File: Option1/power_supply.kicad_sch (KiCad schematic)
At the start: 26 parts, among them U201 uA7812, U202 K7805-500R2_C909663, U203 SY8089AAAC

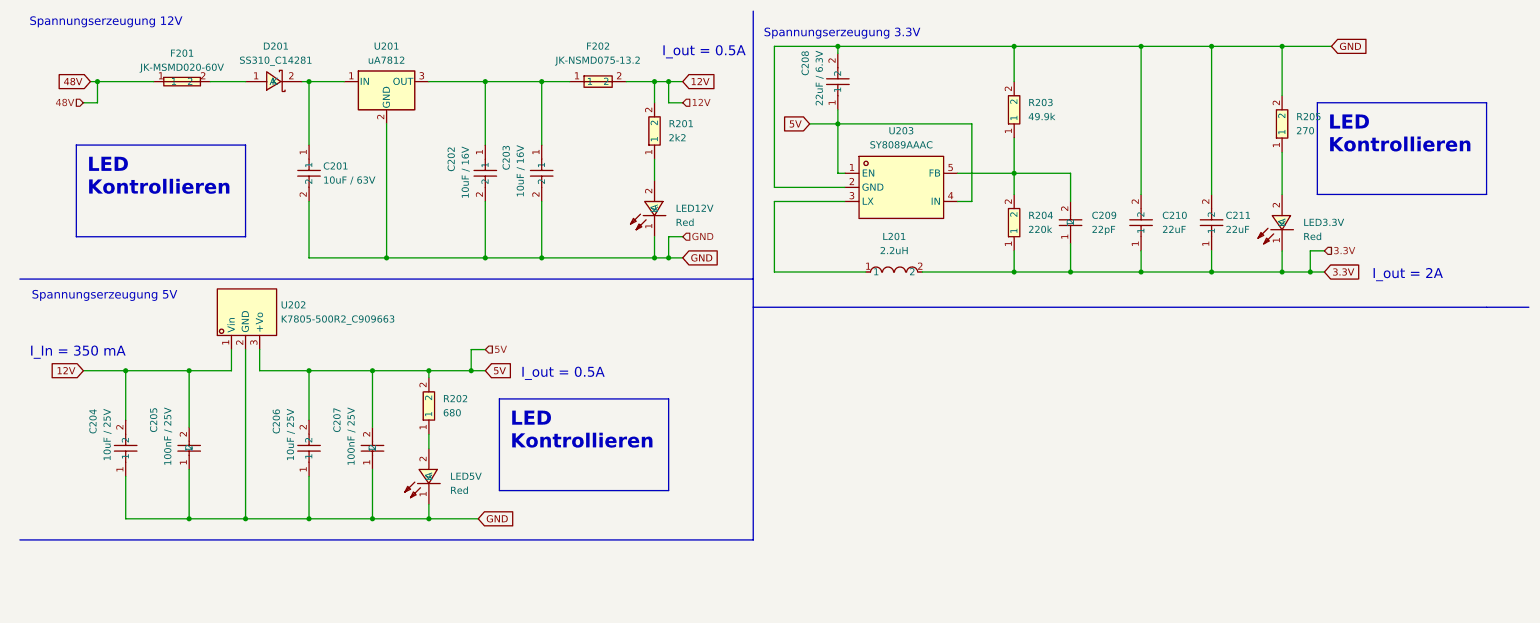
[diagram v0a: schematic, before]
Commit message: SPI Flash hinzugefügt, IN/Outputs vereinheitlicht, USB Flash Möglichkeit hinzugefügt, Display fehtl noch
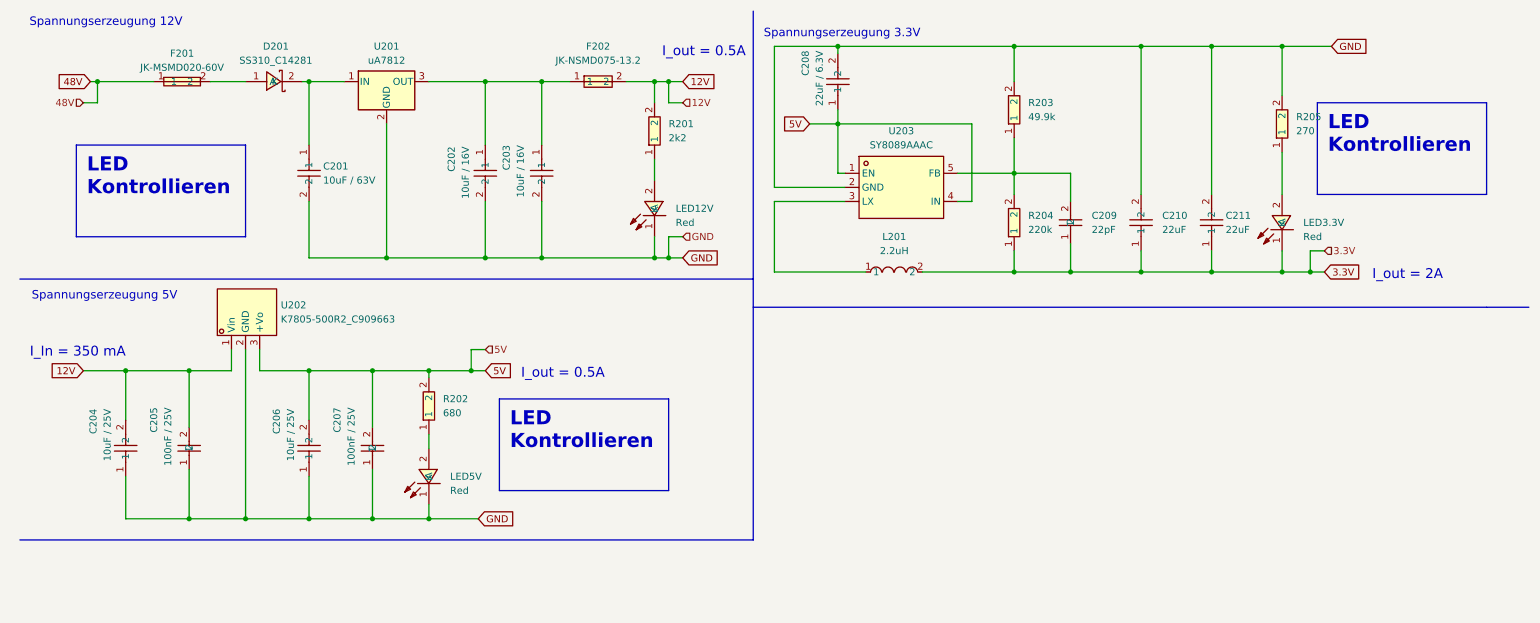
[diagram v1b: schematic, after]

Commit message: Erste issues eingearbeitet
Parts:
- removed LED12V, LED3.3V, LED5V: Red, easyeda2kicad:LED0603-RD, symbol easyeda2kicad:KT-0603R
- removed R201: 2k2, easyeda2kicad:R0603, symbol easyeda2kicad:0603WAF2201T5E
- removed R202: 680, easyeda2kicad:R0603, symbol easyeda2kicad:0603WAF6800T5E
- removed R205: 270, easyeda2kicad:R0603, symbol easyeda2kicad:0603WAF2700T5E
- removed U201: uA7812, symbol Regulator_Linear:uA7812
- added LED12V, LED3V3, LED5V: XL-1608SYGC-06, easyeda2kicad:LED0603-RD_GREEN, symbol EasyEda2KiCad:XL-1608SYGC-06
- added R201: 1.8kΩ, easyeda2kicad:R0603, symbol EasyEda2KiCad:0603WAF1801T5E
- added R202: 560Ω, easyeda2kicad:R0603, symbol EasyEda2KiCad:0603WAF5600T5E
- added R205: 220Ω, easyeda2kicad:R0603, symbol EasyEda2KiCad:0603WAJ0221T5E
- added U201: U7812-500, easyeda2kicad:PWRM-TH_3P-L11.6-W9.0-P2.54, symbol EasyEda2KiCad:U7812-500
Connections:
- net 12V: now also R201.2
- net 3.3V: now also LED3V3.1 (K)
- net 5V: now also R202.2
- net GND: now also LED12V.1 (K), LED5V.1 (K), R205.2, U201.2 (GND)
- net 12V_OUT: now reaches C202.1, C203.1, F202.1
- net 12V_OUT: now also U201.3 (Vout)
- net 48V_FUSED: now reaches C201.1, D201.2 (K)
- net 48V_FUSED: now also U201.1 (Vin)
- new net: LED3V3.2 (A), R205.1
- new net: LED5V.2 (A), R202.1
- new net: LED12V.2 (A), R201.1
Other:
- note added: "5mA - Green"
- moved on the sheet: D201

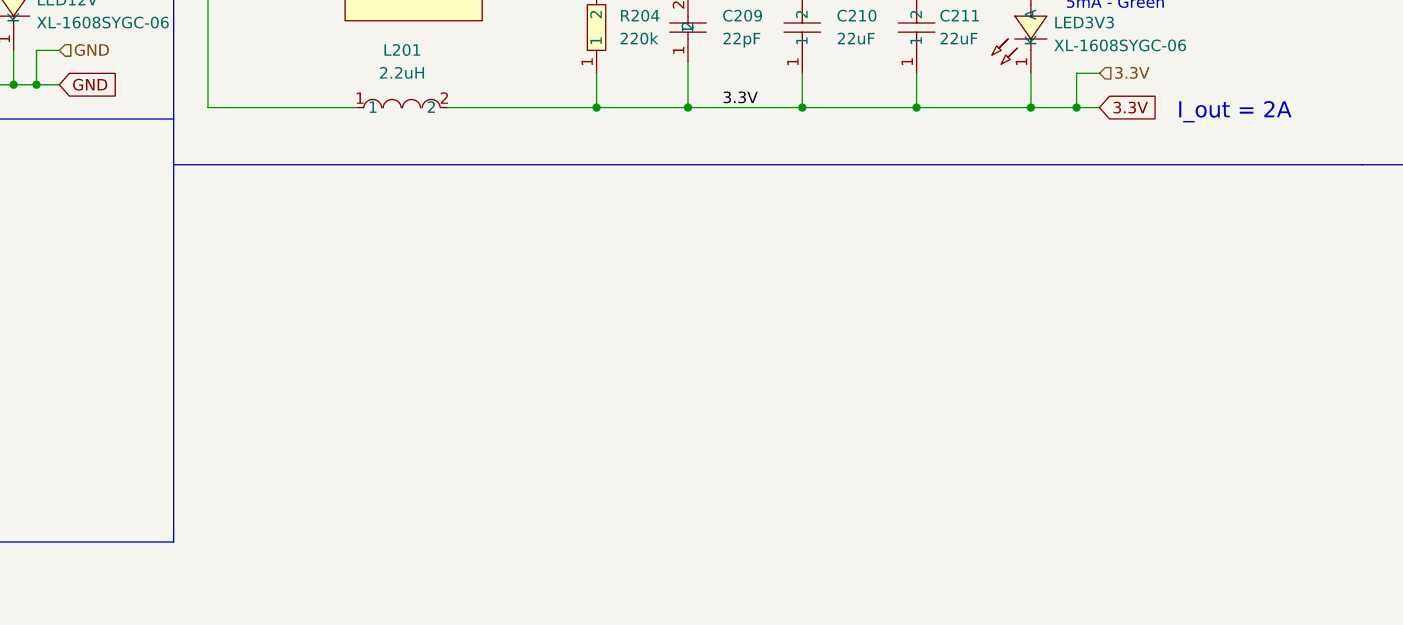
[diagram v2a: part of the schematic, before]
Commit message: Zweite 3V3 Spannungsversorgung für Display hinzugefügt
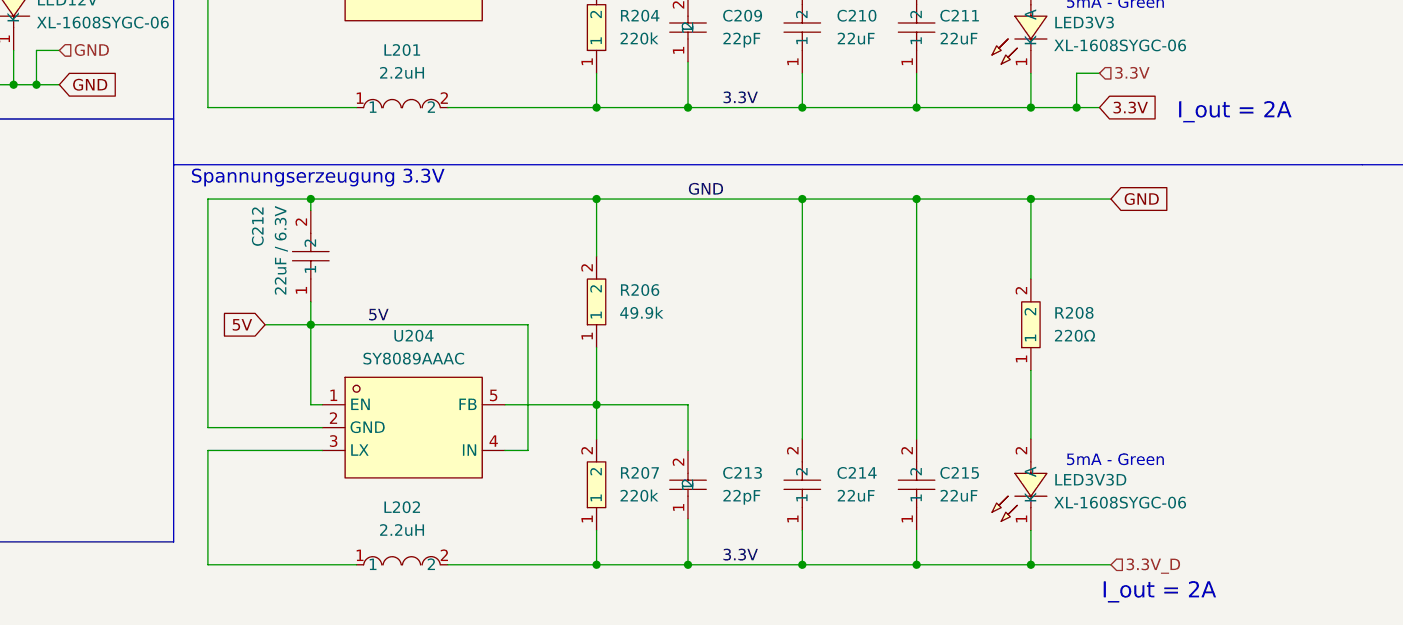
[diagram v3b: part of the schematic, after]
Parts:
- added C212: 22uF / 6.3V, easyeda2kicad:C0603, symbol easyeda2kicad:CL10A226MQ8NRNC
- added C213: 22pF, easyeda2kicad:C0805, symbol easyeda2kicad:CL21C220JBANNNC
- added C214, C215: 22uF, easyeda2kicad:C0805, symbol easyeda2kicad:CL21A226MAQNNNE
- added L202: 2.2uH, easyeda2kicad:IND-SMD_L3.0-W3.0_NR3010, symbol easyeda2kicad:NR3015T2R2M
- added LED3V3D: XL-1608SYGC-06, easyeda2kicad:LED0603-RD_GREEN, symbol EasyEda2KiCad:XL-1608SYGC-06
- added R206: 49.9k, easyeda2kicad:R0603, symbol easyeda2kicad:0603WAF4992T5E
- added R207: 220k, easyeda2kicad:R0603, symbol easyeda2kicad:0603WAF2203T5E
- added R208: 220Ω, easyeda2kicad:R0603, symbol EasyEda2KiCad:0603WAJ0221T5E
- added U204: SY8089AAAC, easyeda2kicad:SOT-23-5_L3.0-W1.7-P0.95-LS2.8-BR, symbol easyeda2kicad:SY8089AAAC
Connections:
- net 3.3V: now also C213.1, C214.1, C215.1, L202.2, LED3V3D.1 (K), R207.1
- net 5V: now also C212.1, U204.1 (EN), U204.4 (IN)
- net GND: now also C212.2, C214.2, C215.2, R206.2, R208.2, U204.2 (GND)
- new net: LED3V3D.2 (A), R208.1
- new net: C213.2, R206.1, R207.2, U204.5 (FB)
- new net: L202.1, U204.3 (LX)

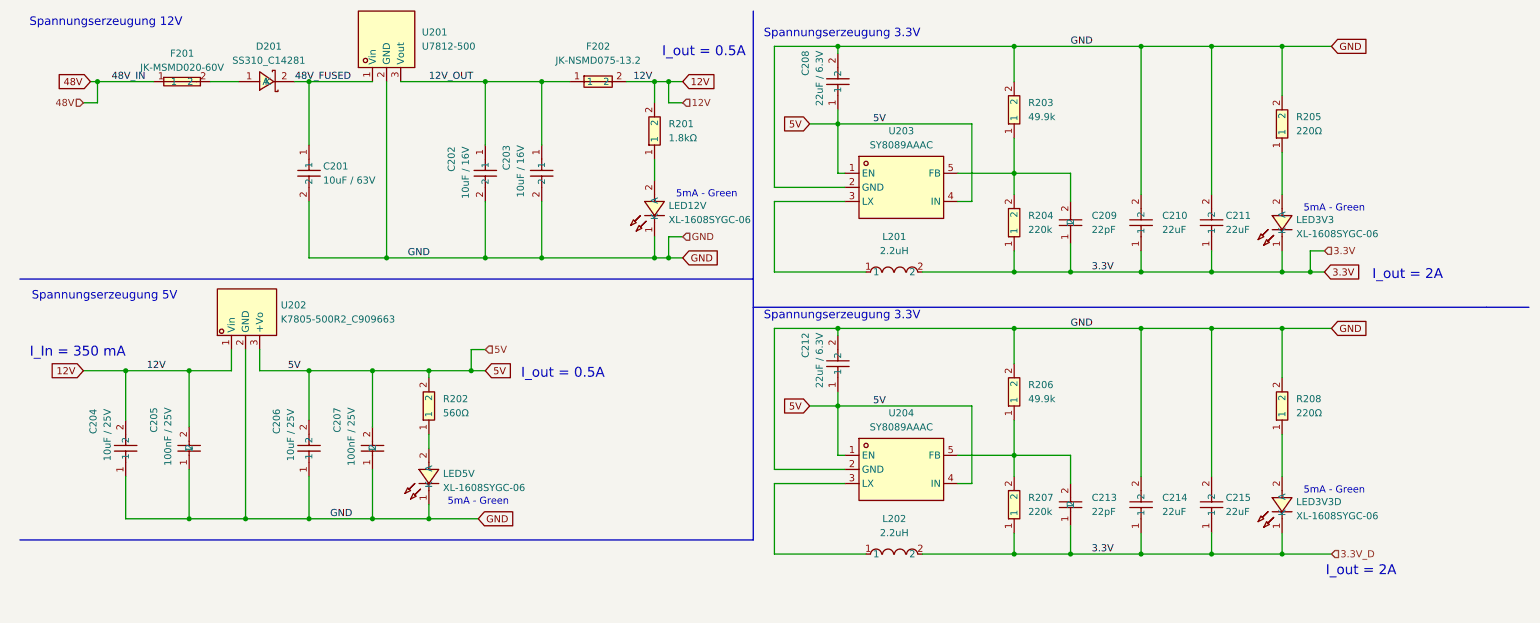
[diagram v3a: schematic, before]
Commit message: USB Schaltung angepasst, Transistoren korrigiert, Stecker ausgetauscht, Dioden hinzugefügt
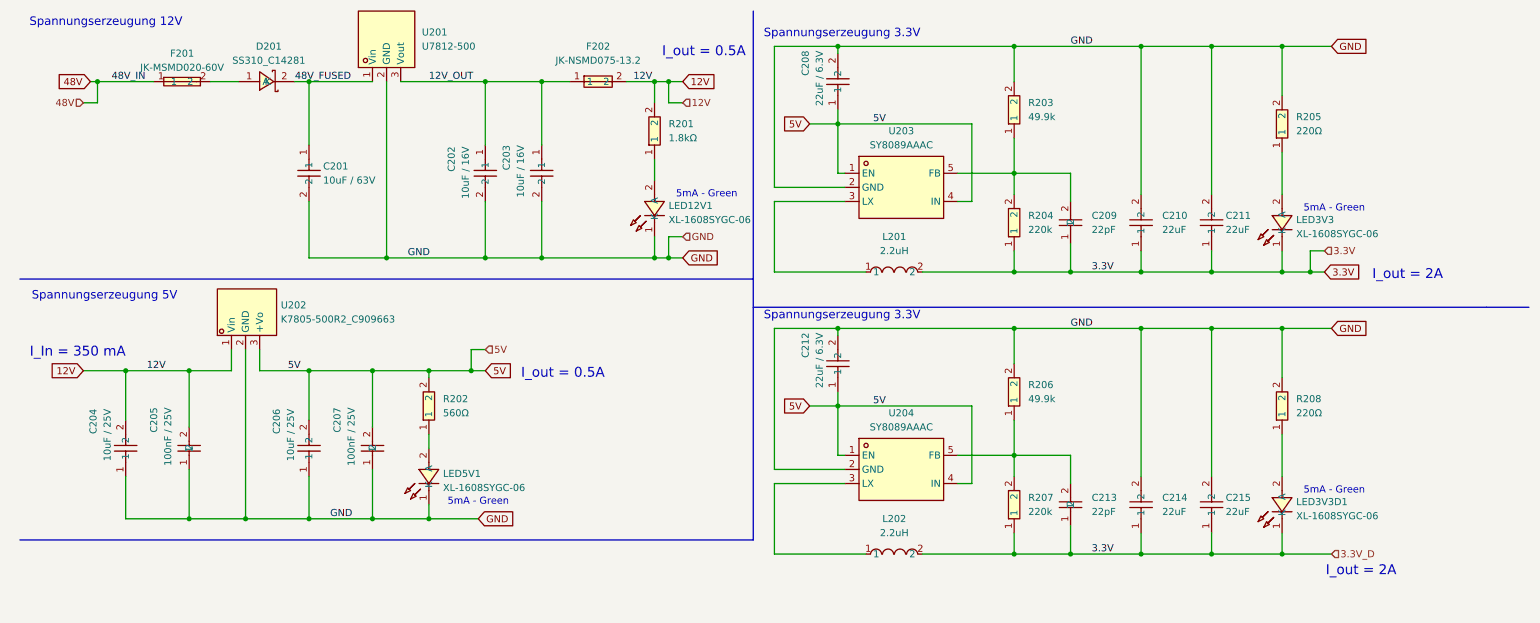
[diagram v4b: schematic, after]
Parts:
- D201: footprint easyeda2kicad:SMB_L4.6-W3.6-LS5.3-R-RD -> easyeda2kicad:SMB_L4.6-W3.6-LS5.3-RD
- renumbered LED12V to LED12V1, LED3V3D to LED3V3D1, LED5V to LED5V1
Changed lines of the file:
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@@
 		(dnp no)
 		(fields_autoplaced yes)
-		(property "Reference" "LED3V3D"
+		(property "Reference" "LED3V3D1"
 			(at 242.57 101.0899 90)
 			(effects
@@
 			(project "Option1"
 				(path "/b9e5f262-9648-4b79-bdd1-af888b822329/ff0aab3a-6ec2-4a6b-b0bf-5e79396b738a"
-					(reference "LED3V3D")
+					(reference "LED3V3D1")
 					(unit 1)
 				)
@@
 			)
 		)
-		(property "Footprint" "easyeda2kicad:SMB_L4.6-W3.6-LS5.3-R-RD"
+		(property "Footprint" "easyeda2kicad:SMB_L4.6-W3.6-LS5.3-RD"
 			(at 57.15 17.78 0)
 			(effects
@@
 		(dnp no)
 		(fields_autoplaced yes)
-		(property "Reference" "LED12V"
+		(property "Reference" "LED12V1"
 			(at 129.54 47.7499 90)
 			(effects
@@
 			(project ""
 				(path "/b9e5f262-9648-4b79-bdd1-af888b822329/ff0aab3a-6ec2-4a6b-b0bf-5e79396b738a"
-					(reference "LED12V")
+					(reference "LED12V1")
 					(unit 1)
 				)
@@
 		(dnp no)
 		(fields_autoplaced yes)
-		(property "Reference" "LED5V"
+		(property "Reference" "LED5V1"
 			(at 88.9 96.0099 90)
 			(effects
@@
 			(project ""
 				(path "/b9e5f262-9648-4b79-bdd1-af888b822329/ff0aab3a-6ec2-4a6b-b0bf-5e79396b738a"
-					(reference "LED5V")
-					(unit 1)
-				)
+					(reference "LED5V1")
+					(unit 1)
+				)

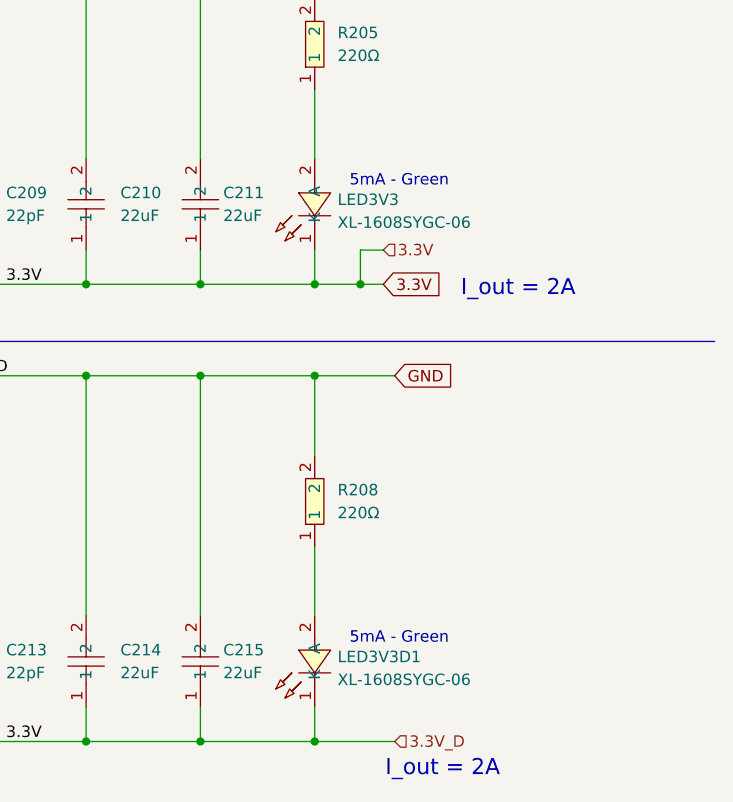
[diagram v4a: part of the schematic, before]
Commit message: Layout für Powersupply, CAN und Stecker hinzugefügt
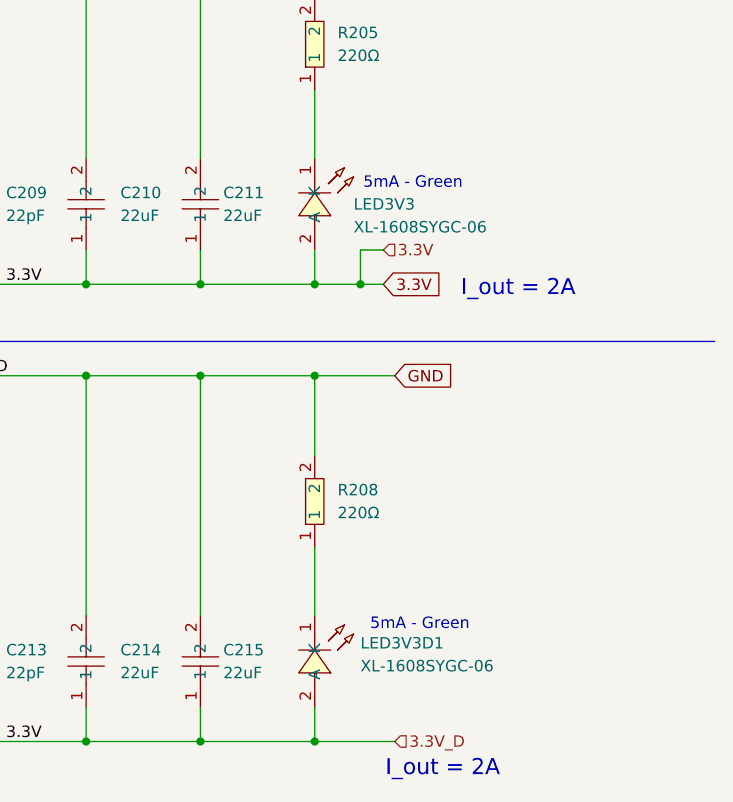
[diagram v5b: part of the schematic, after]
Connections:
- net 3.3V: now also LED3V3.2 (A), LED3V3D1.2 (A); no longer LED3V3.1 (K), LED3V3D1.1 (K)
- net at R205.1: now also LED3V3.1 (K); no longer LED3V3.2 (A)
- net at R208.1: now also LED3V3D1.1 (K); no longer LED3V3D1.2 (A)
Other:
- moved on the sheet: LED3V3, LED3V3D1
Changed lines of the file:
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@@
 	(text "5mA - Green"
 		(exclude_from_sim no)
-		(at 249.428 99.06 0)
+		(at 251.714 97.536 0)
 		(effects
 			(font
@@
 	(text "5mA - Green"
 		(exclude_from_sim no)
-		(at 249.428 48.26 0)
+		(at 250.952 48.514 0)
 		(effects
 			(font
@@
 	(symbol
 		(lib_id "EasyEda2KiCad:XL-1608SYGC-06")
-		(at 240.03 101.6 90)
+		(at 240.03 101.6 270)
 		(unit 1)
 		(exclude_from_sim no)
@@
 		(fields_autoplaced yes)
 		(property "Reference" "LED3V3D1"
-			(at 242.57 101.0899 90)
+			(at 245.11 99.5699 90)
 			(effects
 				(font
 					(size 1.27 1.27)
 				)
-				(justify right)
+				(justify left)
 			)
 		)
 		(property "Value" "XL-1608SYGC-06"
-			(at 242.57 103.6299 90)
+			(at 245.11 102.1099 90)
 			(effects
 				(font
 					(size 1.27 1.27)
 				)
-				(justify right)
+				(justify left)
 			)
 		)
 		(property "Footprint" "easyeda2kicad:LED0603-RD_GREEN"
-			(at 247.65 101.6 0)
+			(at 232.41 101.6 0)
 			(effects
 				(font
@@
 		)
 		(property "LCSC Part" "C965805"
-			(at 250.19 101.6 0)
+			(at 229.87 101.6 0)
 			(effects
 				(font
@@
 	(symbol
 		(lib_id "EasyEda2KiCad:XL-1608SYGC-06")
-		(at 240.03 50.8 90)
+		(at 240.03 50.8 270)
 		(unit 1)
 		(exclude_from_sim no)
@@
 		(on_board yes)
 		(dnp no)
-		(fields_autoplaced yes)
 		(property "Reference" "LED3V3"
-			(at 242.57 50.2899 90)
+			(at 244.348 50.8 90)
 			(effects
 				(font
 					(size 1.27 1.27)
 				)
-				(justify right)
+				(justify left)
 			)
 		)
 		(property "Value" "XL-1608SYGC-06"
-			(at 242.57 52.8299 90)
+			(at 244.348 53.34 90)
 			(effects
 				(font
 					(size 1.27 1.27)
 				)
-				(justify right)
+				(justify left)
 			)
 		)
 		(property "Footprint" "easyeda2kicad:LED0603-RD_GREEN"
-			(at 247.65 50.8 0)
+			(at 232.41 50.8 0)
 			(effects
 				(font
@@
 		)
 		(property "LCSC Part" "C965805"
-			(at 250.19 50.8 0)
+			(at 229.87 50.8 0)
 			(effects
 				(font
